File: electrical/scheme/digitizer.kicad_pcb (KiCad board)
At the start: 4 copper layers, 120 x 120 mm, 253 parts, among them P1 mode, P10 in-2, P11 in-3, P12 in-1, P13 USB_B, P14 screw, P15 screw, P16 screw, P17 screw, P2 ~rst~, P3 ext, P4 trig, P5 trig-mode, P6 swd, P7 out-0, P8 out-1, P9 in-0, U1 AD8672, U10 crystal-4pin, U100 AD8672, U101 AD8672, U11 CP2102, U12 adr4533, U13 BAT54S, U14 adr4533, U15 ADT7410, U16 MCP1703T-3302E/CB, U17 AD7683, U18 NCP3063, U19 ADG5204, U2 AD8672, U20 NCP3063, U21 AD5543, U22 AD5543, U23 AD5543, U24 AD5543, U3 AD8672, U4 AD8672, U5 AD8672, U6 AD8672, U7 AD8672, U8 AD8672, U9 AD8672

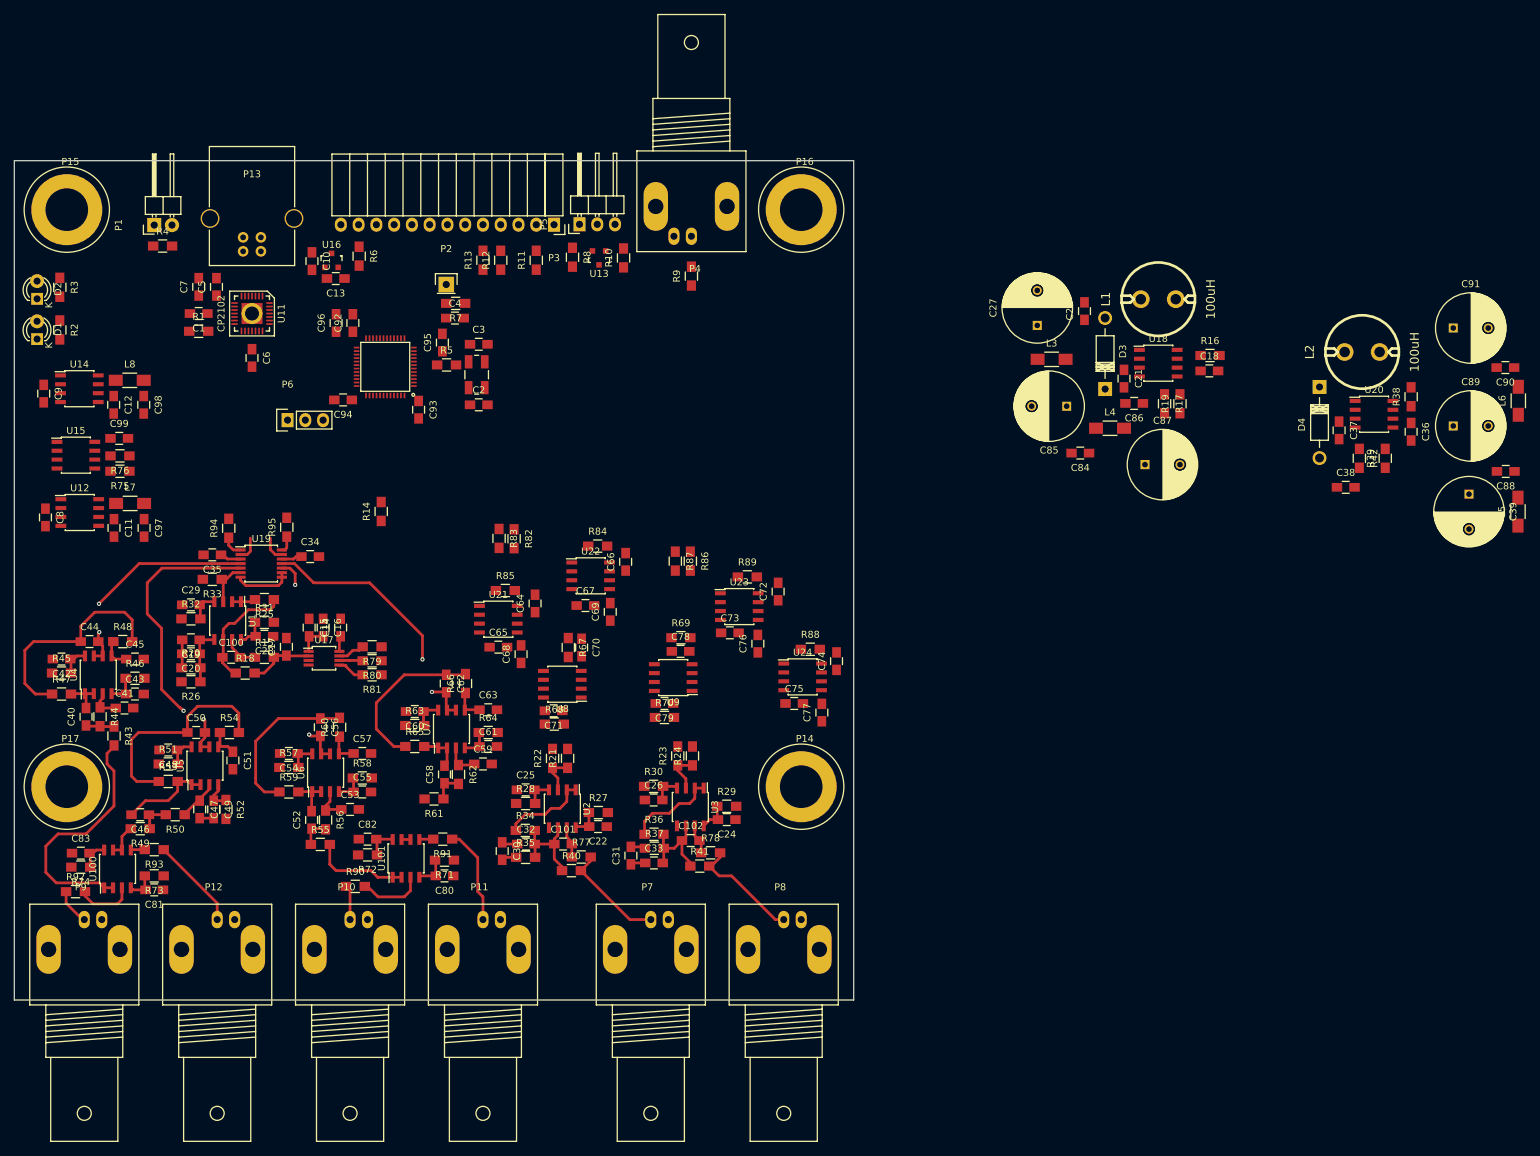
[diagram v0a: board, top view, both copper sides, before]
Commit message: Placed all components. Now routing.
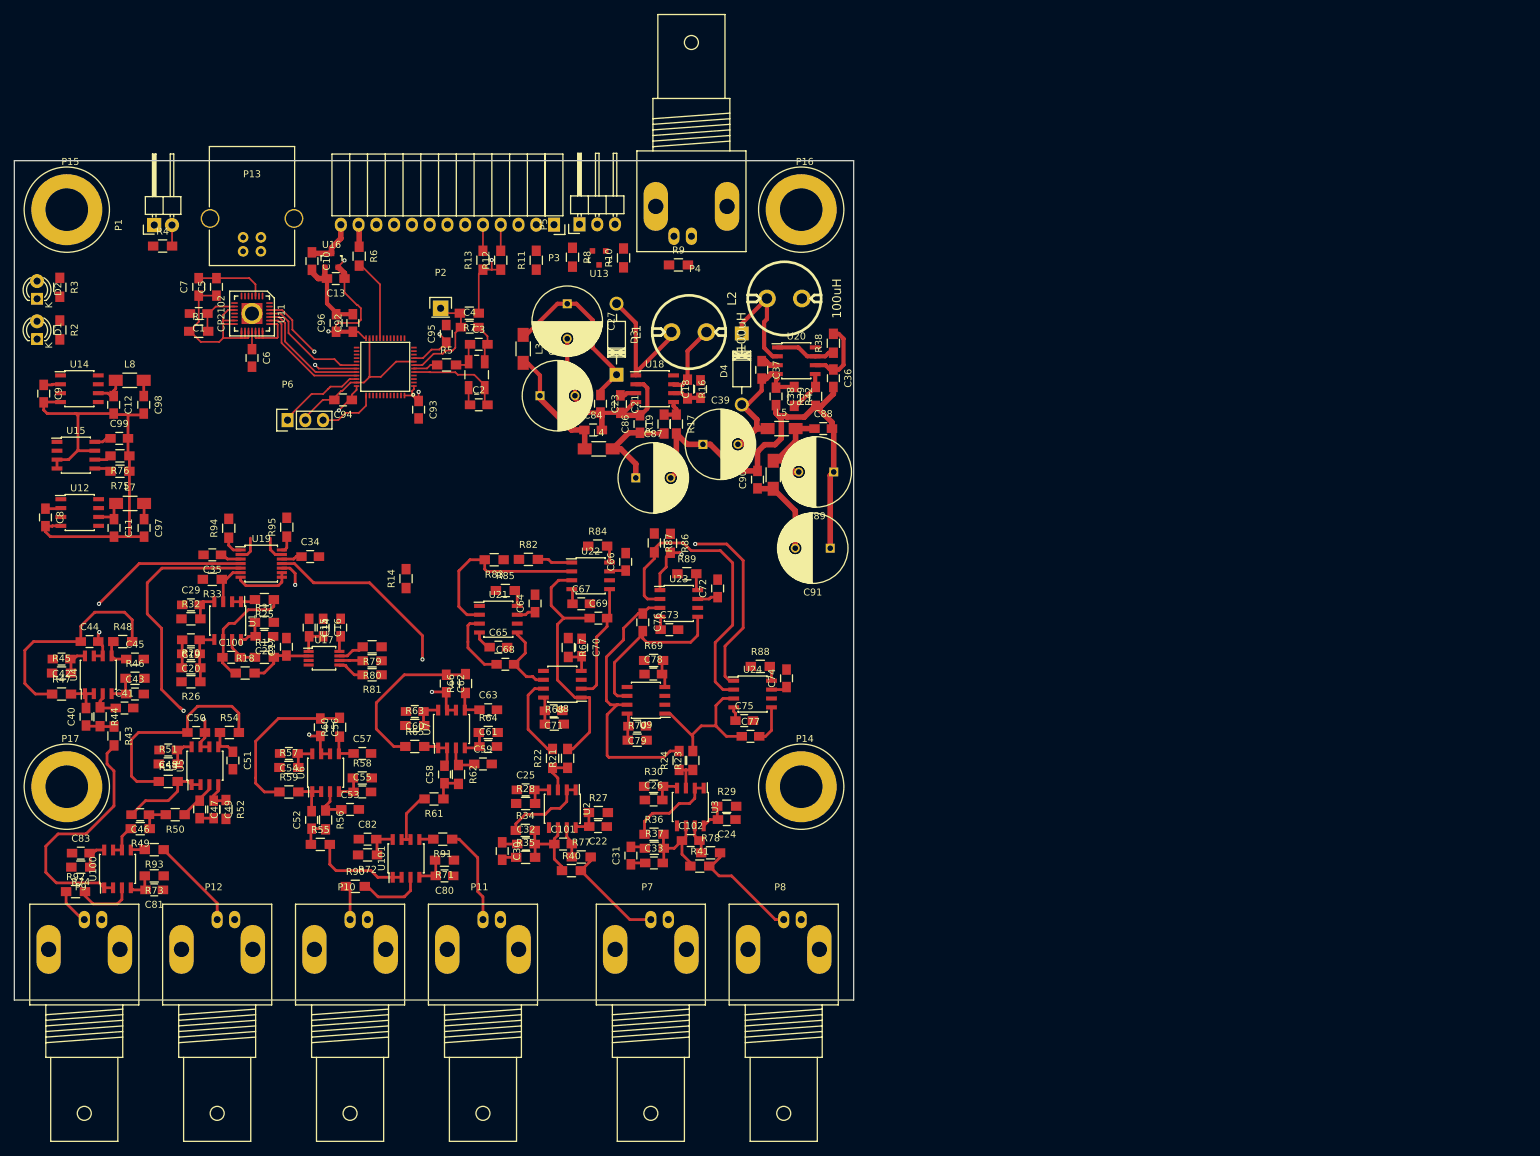
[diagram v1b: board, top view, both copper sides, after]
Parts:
- moved C39 109.8 mm to (158.4, 88.5), turned to 0 degrees
- moved C90 108.1 mm to (166.2, 93.6), turned to 90 degrees
- moved L6 107.0 mm to (168.5, 92.9), turned to 270 degrees
- moved L5 105.9 mm to (169.7, 86.3), turned to 0 degrees
- moved C88 97.8 mm to (175.7, 86.3), turned to 0 degrees
- moved C91 94.5 mm to (176.7, 103.4), turned to 180 degrees
- moved C89 88.8 mm to (177.2, 92.5), turned to 180 degrees
- moved C37 83.0 mm to (166.8, 77.9)
- moved C36 83.0 mm to (177.1, 79.1)
- moved D4 83.0 mm to (164.0, 72.7)
- moved L2 83.0 mm to (170.1, 67.7)
- moved R38 83.0 mm to (177.1, 74.1)
- moved U20 83.0 mm to (171.8, 76.6)
- moved C38 82.5 mm to (168.9, 81.7), turned to 270 degrees
- moved R39 81.9 mm to (174.6, 81.7)
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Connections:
- U12 pad 3: VDD -> (no net)
- U14 pad 3: VDD -> (no net)
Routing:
- net GND: track 0.00 -> 220.5 mm
- net VDD: track 5.71 -> 171.4 mm, vias 0 -> 6
- net /dac-v-1/mosi: track 0.00 -> 43.6 mm
- net /dac-v-1/out-2: track 0.00 -> 39.7 mm
- net /dac-v-1/sck: track 0.00 -> 37.2 mm, vias 0 -> 2
- net /dac-v-0/out-1: track 0.00 -> 36.1 mm
- net Net-(C37-Pad2): track 0.00 -> 28.8 mm
- net /dac-v-0/mosi: track 0.00 -> 26.8 mm
- net /Vbus: track 0.00 -> 26.5 mm
- net Net-(C23-Pad1): track 0.00 -> 25.8 mm
- net Net-(C76-Pad2): track 0.00 -> 24.8 mm
- net /dac-v-0/out-2: track 0.00 -> 22.2 mm
- net /dac-v-1/out-1: track 0.00 -> 21.7 mm
- net Net-(D3-Pad2): track 0.00 -> 19.3 mm
- net /txd: track 0.00 -> 17.8 mm, vias 0 -> 2
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
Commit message: a
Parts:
- moved C77 6.65 mm to (159.9, 126.3), turned to 270 degrees
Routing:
- net /Vbus: track 26.5 -> 157.0 mm, vias 0 -> 3
- net /dac-cs-2: track 0.00 -> 95.8 mm, vias 0 -> 2
- net /dac-cs-3: track 0.00 -> 71.2 mm, vias 0 -> 2
- net /dac-sck: track 0.00 -> 51.8 mm, vias 0 -> 2
- net /dac-mosi: track 0.00 -> 49.6 mm, vias 0 -> 2
- net /adc-mux-0: track 0.00 -> 48.0 mm, vias 0 -> 2
- net /adc-mux-1: track 0.00 -> 43.1 mm, vias 0 -> 2
- net /dac-cs-0: track 0.00 -> 33.4 mm
- net VDD: track 171.4 -> 203.9 mm, vias 6 -> 7
- net GND: track 220.5 -> 250.8 mm
- net /adc-cs: track 0.00 -> 27.1 mm, vias 0 -> 1
- net /adc-miso: track 0.00 -> 25.2 mm, vias 0 -> 1
- net /adc-sck: track 0.00 -> 21.4 mm, vias 0 -> 1
- net Net-(C77-Pad2): track 5.40 -> 21.7 mm
- net Net-(P13-Pad3): track 0.00 -> 9.08 mm
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
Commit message: a
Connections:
- U11 pad 1: Net-(U11-Pad1) -> (no net)
- stm321 pad 18: /gpio-1 -> /gpio-3
- stm321 pad 19: /gpio-2 -> /gpio-4
- stm321 pad 2: /gpio-0 -> /led-1
- stm321 pad 4: /led-1 -> /gpio-0
- stm321 pad 41: /gpio-3 -> /gpio-2
- stm321 pad 45: /gpio-4 -> /gpio-1
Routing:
- net GND: track 250.8 -> 373.2 mm
- net /dac-cs-1: track 0.00 -> 54.7 mm, vias 0 -> 4
- net /i2c1-scl: track 3.73 -> 47.0 mm, vias 0 -> 1
- net /i2c1-sda: track 3.73 -> 43.6 mm, vias 0 -> 1
- net /gpio-0: track 0.00 -> 31.5 mm, vias 0 -> 2
- net /gpio-1: track 0.00 -> 31.5 mm, vias 0 -> 2
- net /gpio-4: track 0.00 -> 30.3 mm, vias 0 -> 2
- net /gpio-2: track 0.00 -> 30.0 mm, vias 0 -> 2
- net /dac-sck: track 51.8 -> 77.7 mm, vias 2 -> 4
- net /suspend: track 0.00 -> 24.7 mm, vias 0 -> 2
- net Net-(P4-Pad1): track 0.00 -> 22.1 mm
- net /dac-mosi: track 49.6 -> 71.5 mm, vias 2 -> 4
- net VDD: track 203.9 -> 221.9 mm
- net /gpio-3: track 0.00 -> 16.6 mm
- net /dac-cs-0: track 33.4 -> 41.2 mm
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
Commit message: a
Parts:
- moved R14 9.85 mm to (108.0, 102.0)
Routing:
- net /led-0: track 0.00 -> 73.4 mm, vias 0 -> 2
- net /led-1: track 0.00 -> 72.6 mm, vias 0 -> 2
- net /boot0: track 5.40 -> 59.8 mm
- net /adc-miso: track 25.2 -> 74.0 mm, vias 1 -> 2
- net /adc-sck: track 21.4 -> 63.8 mm, vias 1 -> 2
- net /gpio-4: track 30.3 -> 70.9 mm
- net /adc-cs: track 27.1 -> 67.5 mm, vias 1 -> 2
- net /rx-2: track 0.00 -> 32.9 mm, vias 0 -> 1
- net /tx-2: track 0.00 -> 31.2 mm, vias 0 -> 1
- net GND: track 373.2 -> 394.9 mm
- net /i2c1-scl: track 47.0 -> 51.1 mm
- net /i2c1-sda: track 43.6 -> 47.6 mm
- net Net-(D2-Pad1): track 0.00 -> 3.37 mm
- net Net-(D1-Pad1): track 0.00 -> 3.27 mm
- added copper zone on B.Cu, net GND
- added copper zone on F.Cu, net GND
- added copper zone on In1.Cu, net GND
- added copper zone on In2.Cu, net GND
- added copper zone on B.Cu, net GNDA
- added copper zone on F.Cu, net GNDA
- added copper zone on In1.Cu, net GNDA
- added copper zone on In2.Cu, net GNDA

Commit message: Routing...
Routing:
- net GNDA: track 14.0 -> 471.5 mm
- net GND: track 394.9 -> 762.2 mm, vias 0 -> 2
- net /dac-v-0/dac-ref: track 15.4 -> 228.7 mm, vias 0 -> 3
- net VDD: track 221.9 -> 408.5 mm, vias 7 -> 9
- net /adc-ref: track 6.43 -> 99.1 mm, vias 0 -> 3
- net /Vbus: track 157.0 -> 235.2 mm, vias 3 -> 4
- net /i2c1-sda: track 47.6 -> 100.8 mm, vias 1 -> 3
- net /i2c1-scl: track 51.1 -> 103.1 mm, vias 1 -> 3
- net Net-(D3-Pad2): track 19.3 -> 17.2 mm
- net /boot0: track 59.8 -> 57.7 mm

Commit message: Routing...
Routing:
- net GNDA: track 471.5 -> 941.1 mm, vias 0 -> 37
- net /dac-v-0/dac-ref: track 228.7 -> 448.3 mm, vias 3 -> 5
- net GND: track 762.2 -> 813.0 mm, vias 2 -> 4
- net /dac-v-0/sck: track 5.03 -> 23.5 mm, vias 0 -> 2
- net /dac-v-0/out-2: track 22.2 -> 29.2 mm
- net /adc-ref: track 99.1 -> 101.1 mm

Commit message: a
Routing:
- net /dac-v-0/v-: track 23.3 -> 606.2 mm, vias 0 -> 8
- net GND: track 813.0 -> 1043.4 mm, vias 4 -> 6
- net /dac-v-0/v+: track 17.5 -> 195.2 mm, vias 0 -> 2
- net VDD: track 408.5 -> 417.4 mm
- net /input-filter-attenuator-3/out: track 39.0 -> 41.1 mm
- net /dac-v-0/dac-ref: track 448.3 -> 447.1 mm
- net GNDA: track 941.1 -> 941.8 mm

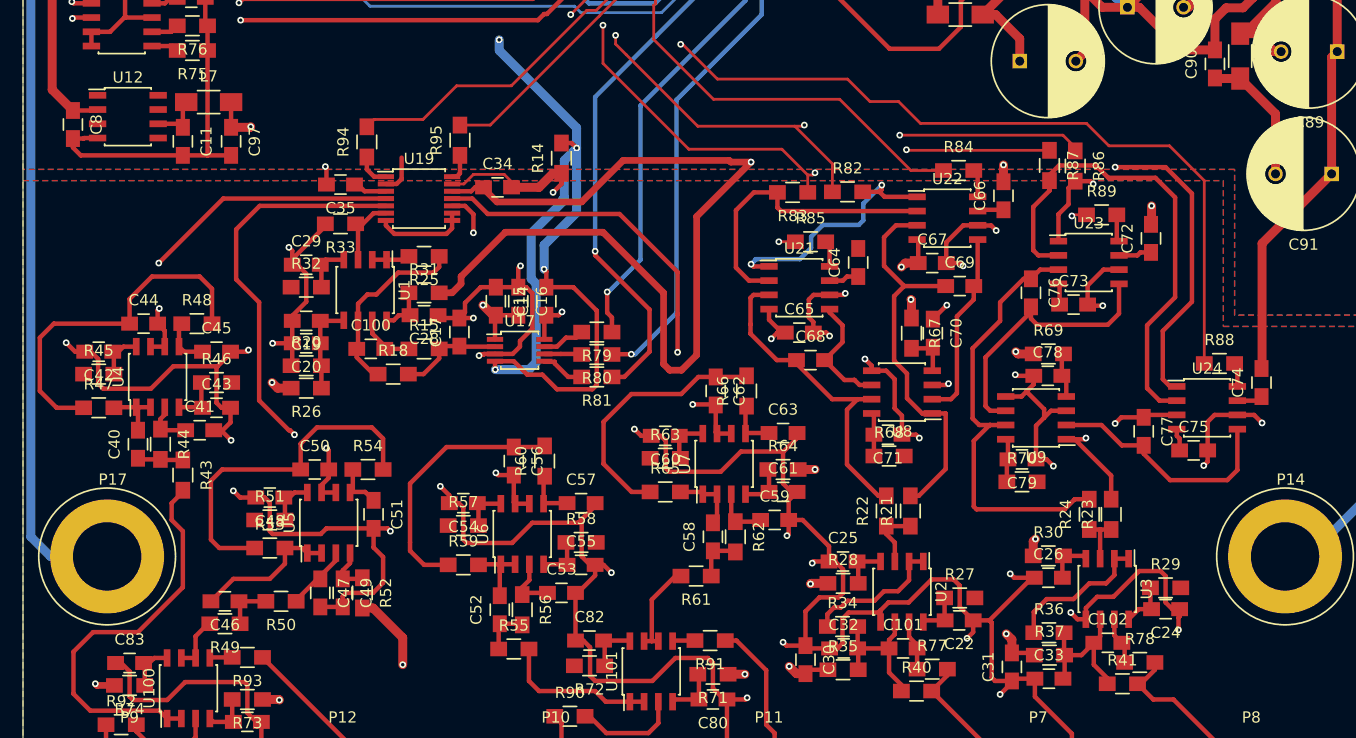
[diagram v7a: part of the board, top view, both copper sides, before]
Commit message: Routing completed in the very first approximation.
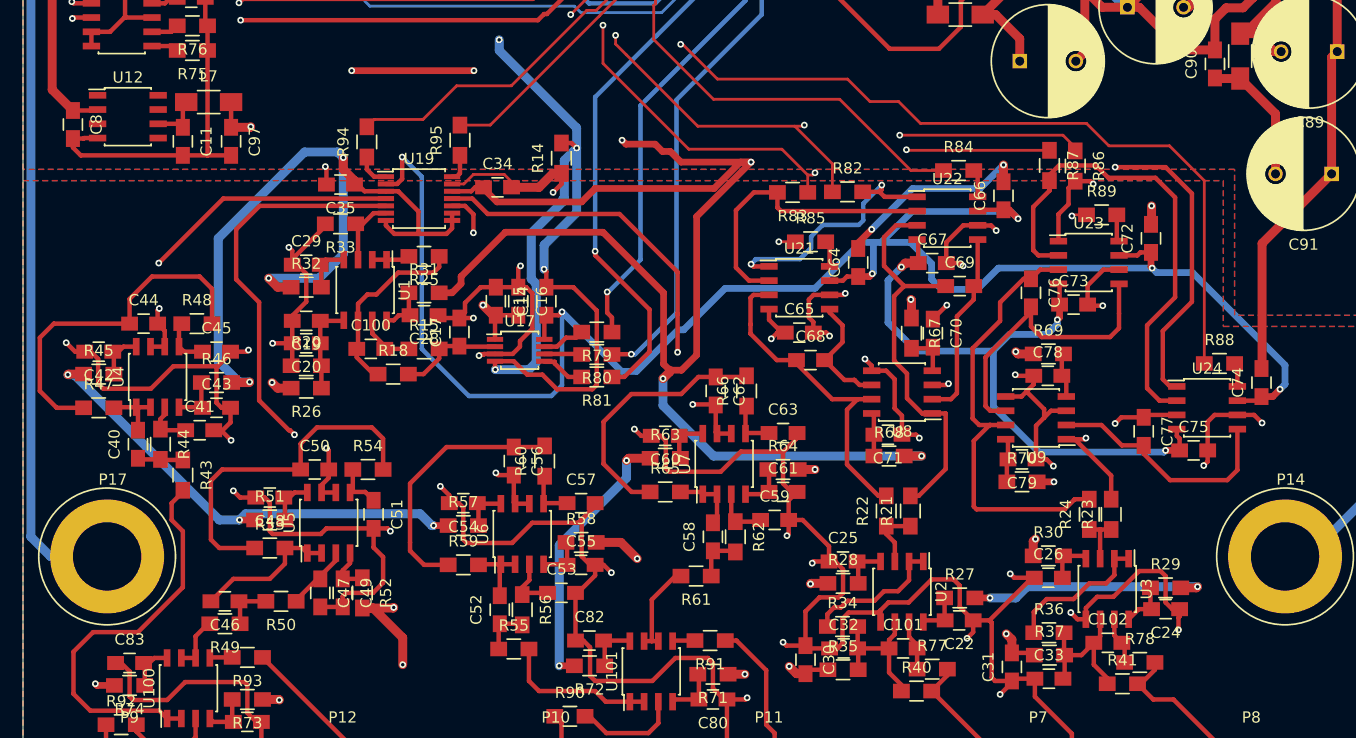
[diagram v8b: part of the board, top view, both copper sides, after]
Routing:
- net /dac-v-0/v+: track 195.2 -> 494.6 mm, vias 2 -> 15
- net /dac-v-0/v-: track 606.2 -> 789.2 mm, vias 8 -> 13
- net VDD: track 417.4 -> 560.0 mm, vias 9 -> 14
- net /dac-v-0/dac-ref: track 447.1 -> 499.5 mm, vias 5 -> 7
- net GND: track 1043.4 -> 1059.8 mm, vias 6 -> 7
- net GNDA: track 941.8 -> 939.5 mm
- net Net-(C76-Pad2): track 24.8 -> 26.8 mm
- net /adc-ref: track 101.1 -> 100.5 mm
